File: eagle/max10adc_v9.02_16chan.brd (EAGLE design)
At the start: 170 x 79 mm, 533 parts, among them IC1 MAX11115AUT+T, IC10 MAX11115AUT+T, IC11 MAX11115AUT+T, IC12 MAX11115AUT+T, IC13 MAX11115AUT+T, IC14 MAX11115AUT+T, IC15 MAX11115AUT+T, IC16 MAX11115AUT+T, IC2 MAX11115AUT+T, IC21 MAX11115AUT+T, IC22 MAX11115AUT+T, IC23 MAX11115AUT+T, IC24 MAX11115AUT+T, IC3 MAX11115AUT+T, IC4 MAX11115AUT+T, IC9 MAX11115AUT+T, K1 AQY21SOP, K10 AQY21SOP, K11 AQY21SOP, K12 AQY21SOP, K13 AQY21SOP, K14 AQY21SOP, K15 AQY21SOP, K16 AQY21SOP, K21 AQY21SOP, K22 AQY21SOP, K23 AQY21SOP, K24 AQY21SOP, K3 AQY21SOP, K5 AQY21SOP, K6 AQY21SOP, K9 AQY21SOP, U340G CH340G, X1 LTI-SASF54GT, X10 LTI-SASF54GT, X11 LTI-SASF54GT, X12 LTI-SASF54GT, X13 LTI-SASF54GT, X14 LTI-SASF54GT, X15 LTI-SASF54GT, X16 LTI-SASF54GT, X21 LTI-SASF54GT, X22 LTI-SASF54GT, X23 LTI-SASF54GT, X24 LTI-SASF54GT, X4 LTI-SASF54GT, X5 LTI-SASF54GT, X6 LTI-SASF54GT, X9 LTI-SASF54GT, Y1 ABL-12.000MHZ-B2

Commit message: MAX11105
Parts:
- IC1, IC10, IC11, IC12, IC13, IC14, IC15, IC16, IC2, IC21, IC22, IC23, IC24, IC3, IC4, IC9: value MAX11115AUT+T -> MAX11105AUT+T

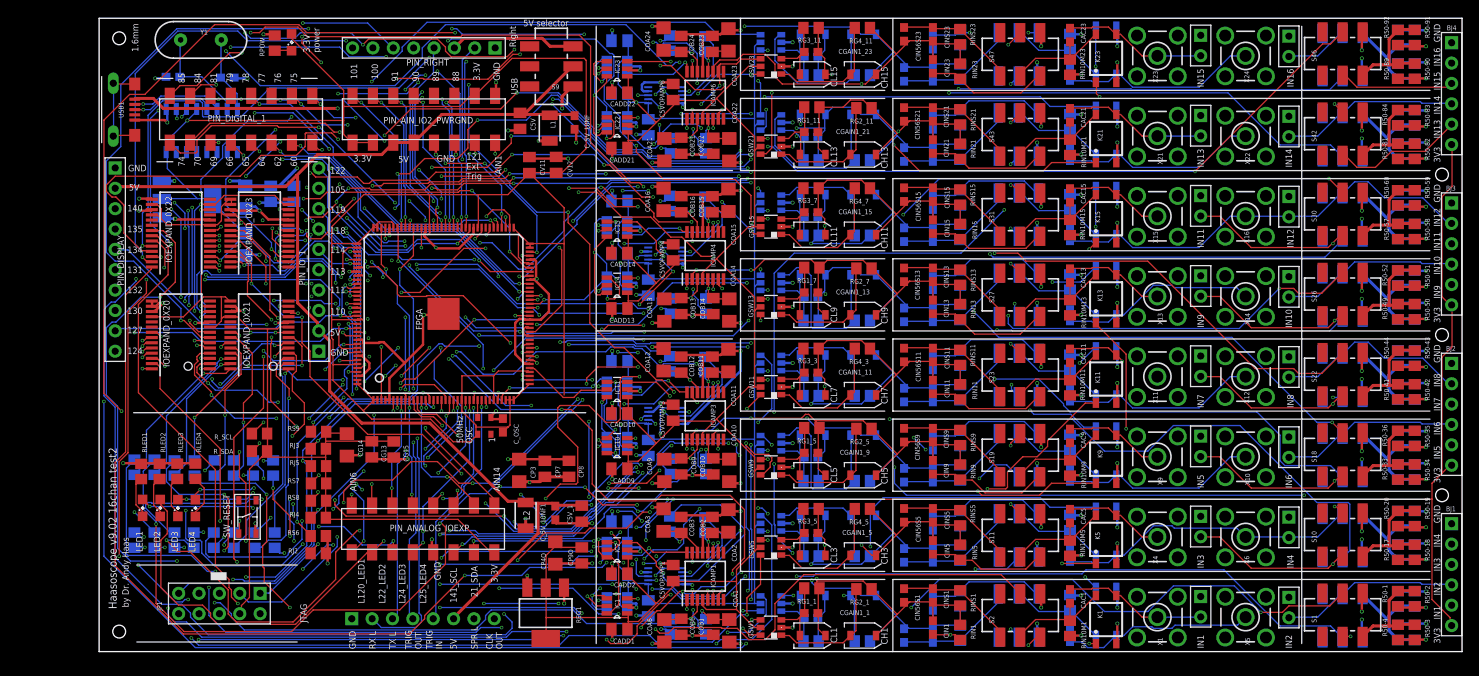
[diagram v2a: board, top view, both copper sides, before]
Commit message: with 24pF fixed caps
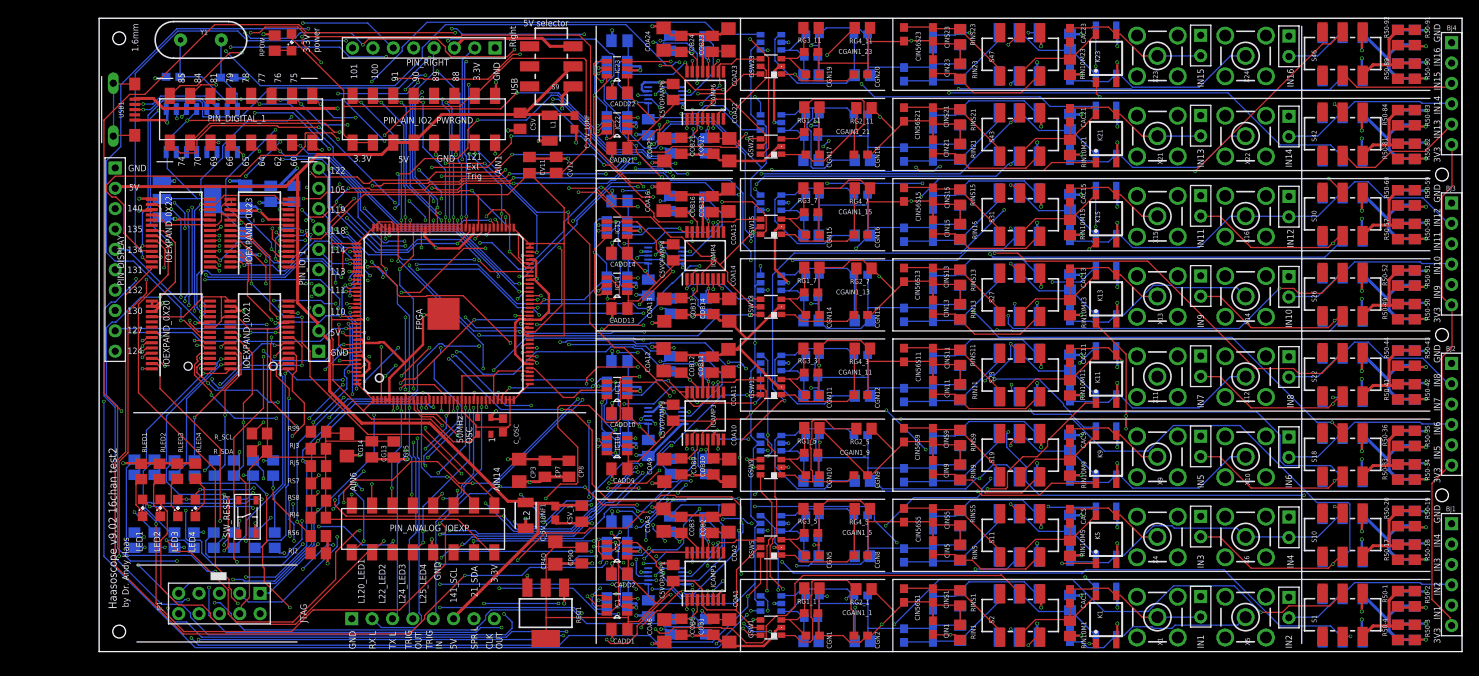
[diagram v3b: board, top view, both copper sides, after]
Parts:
- removed CH1, CH10, CH11, CH12, CH13, CH14, CH15, CH16, CH2, CH3, CH4, CH5, CH6, CH7, CH8, CH9, CL1, CL10, CL11, CL12, CL13, CL14, CL15, CL16, CL2, CL3, CL4, CL5, CL6, CL7, CL8, CL9: 8-45pF, SparkFun-Passives:CTZ3
- added CGN1, CGN10, CGN11, CGN12, CGN13, CGN14, CGN15, CGN16, CGN17, CGN18, CGN19, CGN2, CGN20, CGN21, CGN22, CGN23, CGN24, CGN25, CGN26, CGN27, CGN28, CGN29, CGN3, CGN30, CGN31, CGN32, CGN4, CGN5, CGN6, CGN7, CGN8, CGN9: 24pF, rcl@1:C0603
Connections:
- net CGAIN1: now also CGN1.2; no longer CL1.-
- net CGAIN10: now also CGN8.2; no longer CH3.-
- net CGAIN11: now also CGN6.1; no longer CL4.-
- net CGAIN12: now also CGN7.2; no longer CH4.-
- net CGAIN17: now also CGN10.2; no longer CL5.-
- net CGAIN18: now also CGN9.2; no longer CH5.-
- net CGAIN19: now also CGN22.2; no longer CL6.-
- net CGAIN2: now also CGN2.2; no longer CH1.-
- net CGAIN20: now also CGN21.2; no longer CH6.-
- net CGAIN21: now also CGN11.1; no longer CL7.-
- net CGAIN22: now also CGN12.1; no longer CH7.-
- net CGAIN23: now also CGN23.1; no longer CL8.-
- net CGAIN24: now also CGN24.1; no longer CH8.-
- net CGAIN25: now also CGN14.2; no longer CL9.-
- net CGAIN26: now also CGN13.2; no longer CH9.-
- net CGAIN27: now also CGN26.2; no longer CL10.-
- net CGAIN28: now also CGN25.2; no longer CH10.-
- net CGAIN29: now also CGN15.1; no longer CL11.-
- net CGAIN30: now also CGN16.1; no longer CH11.-
- net CGAIN31: now also CGN27.1; no longer CL12.-
- net CGAIN32: now also CGN28.1; no longer CH12.-
- net CGAIN41: now also CGN18.2; no longer CL13.-
- net CGAIN42: now also CGN17.2; no longer CH13.-
- net CGAIN43: now also CGN30.2; no longer CL14.-
- net CGAIN44: now also CGN29.2; no longer CH14.-
- net CGAIN45: now also CGN19.1; no longer CL15.-
- net CGAIN46: now also CGN20.1; no longer CH15.-
- net CGAIN47: now also CGN31.1; no longer CL16.-
- net CGAIN48: now also CGN32.1; no longer CH16.-
- net CGAIN5: now also CGN4.2; no longer CL2.-
- net CGAIN6: now also CGN3.2; no longer CH2.-
- net CGAIN9: now also CGN5.1; no longer CL3.-
- net INAMINUS1: now also CGN1.1, CGN2.1; no longer CH1.+, CL1.+
- net INAMINUS10: now also CGN25.1, CGN26.1; no longer CH10.+, CL10.+
- net INAMINUS11: now also CGN15.2, CGN16.2; no longer CH11.+, CL11.+
- net INAMINUS12: now also CGN27.2, CGN28.2; no longer CH12.+, CL12.+
- net INAMINUS13: now also CGN17.1, CGN18.1; no longer CH13.+, CL13.+
- net INAMINUS14: now also CGN29.1, CGN30.1; no longer CH14.+, CL14.+
- net INAMINUS15: now also CGN19.2, CGN20.2; no longer CH15.+, CL15.+
- net INAMINUS16: now also CGN31.2, CGN32.2; no longer CH16.+, CL16.+
- net INAMINUS2: now also CGN3.1, CGN4.1; no longer CH2.+, CL2.+
- net INAMINUS3: now also CGN5.2, CGN8.1; no longer CH3.+, CL3.+
- net INAMINUS4: now also CGN6.2, CGN7.1; no longer CH4.+, CL4.+
- net INAMINUS5: now also CGN10.1, CGN9.1; no longer CH5.+, CL5.+
- net INAMINUS6: now also CGN21.1, CGN22.1; no longer CH6.+, CL6.+
- net INAMINUS7: now also CGN11.2, CGN12.2; no longer CH7.+, CL7.+
- net INAMINUS8: now also CGN23.2, CGN24.2; no longer CH8.+, CL8.+
- net INAMINUS9: now also CGN13.1, CGN14.1; no longer CH9.+, CL9.+
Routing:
- net VCCA: track 570.5 -> 518.4 mm, vias 1 -> 8
- net GND: track 607.2 -> 641.1 mm, vias 202 -> 188
- net E_SS10: track 120.3 -> 134.1 mm, vias 7 -> 10
- net CGAIN41: track 9.37 -> 21.5 mm
- net E_GSW5: track 146.6 -> 134.8 mm, vias 5 -> 4
- net INAMINUS11: track 52.2 -> 63.1 mm
- net CGAIN24: track 14.8 -> 25.0 mm
- net CGAIN32: track 14.8 -> 25.0 mm
- net N$8: track 131.7 -> 141.7 mm, vias 4 -> 6
- net E_50SW15: track 198.4 -> 208.4 mm, vias 7 -> 8
- net INAMINUS13: track 65.3 -> 55.8 mm, vias 2 -> 3
- net E_SS12: track 101.9 -> 110.8 mm, vias 5 -> 6
- net CGAIN2: track 15.6 -> 24.4 mm
- net CGAIN18: track 15.6 -> 23.6 mm
- net CGAIN28: track 23.5 -> 15.6 mm
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
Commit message: test3
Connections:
- net N$48 renamed 5VC3
- net N$49 renamed 5VC5
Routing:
- net GND: track 641.1 -> 414.5 mm, vias 188 -> 258
- net +3V3: track 456.1 -> 364.5 mm, vias 2 -> 15
- net E_GSW10: track 86.8 -> 156.9 mm, vias 7 -> 4
- net E_GSW5: track 134.8 -> 87.9 mm, vias 4 -> 6
- net E_GSW11: track 98.4 -> 144.5 mm, vias 8 -> 3
- net E_50SW2: track 204.0 -> 248.9 mm, vias 6 -> 10
- net E_50SW6: track 244.1 -> 203.1 mm, vias 6 -> 7
- net E_50SW7: track 205.3 -> 165.1 mm, vias 6 -> 8
- net E_SS4: track 176.9 -> 137.6 mm, vias 7 -> 8
- net E_GSW7: track 103.9 -> 142.4 mm, vias 3 -> 5
- net E_50SW10: track 152.8 -> 190.8 mm, vias 7 -> 6
- net VCCA: track 518.4 -> 556.3 mm, vias 8 -> 1
- net E_SS10: track 134.1 -> 96.4 mm, vias 10 -> 6
- net N$37: track 134.5 -> 170.7 mm
- net E_GSW13: track 131.4 -> 96.1 mm, vias 6 -> 9
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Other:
- board text added: "Haasoscope v9.02 16chan test3"
- board text removed: "Haasoscope v9.02 16chan test2"

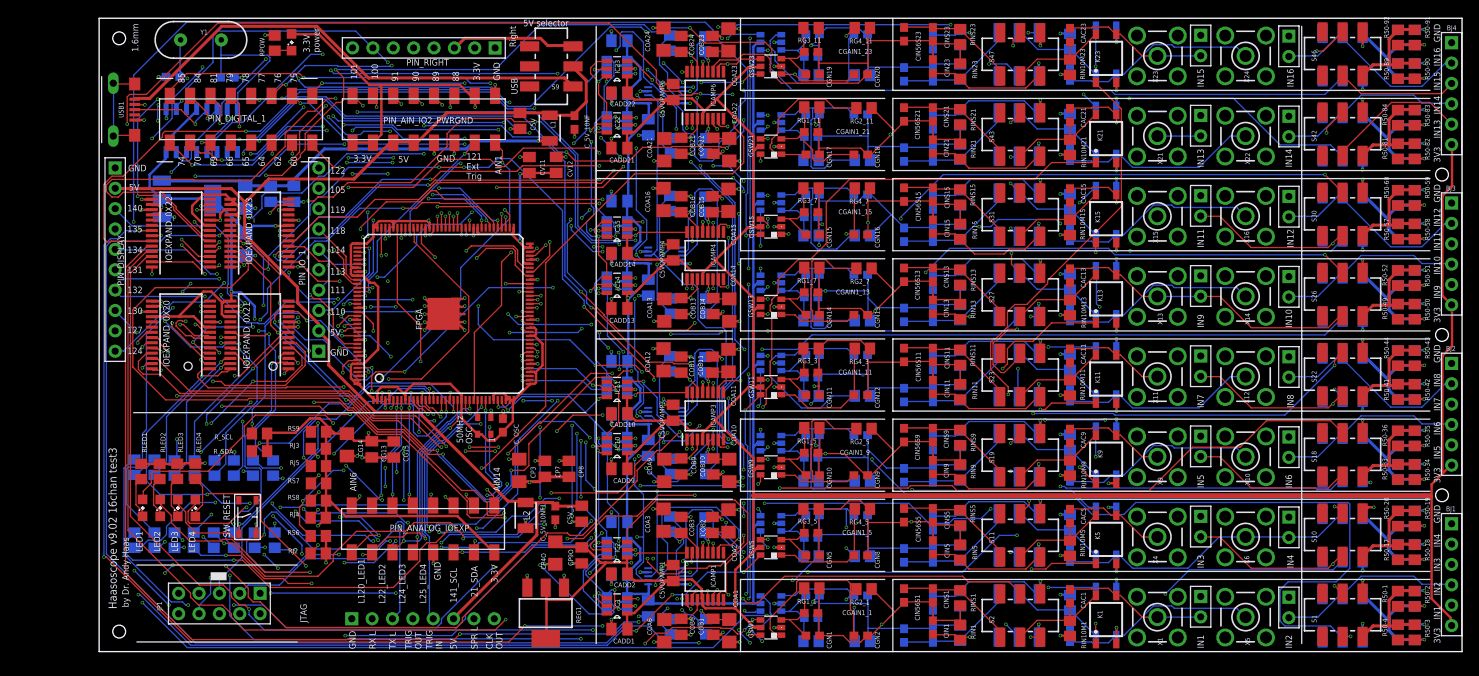
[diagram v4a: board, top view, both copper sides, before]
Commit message: front panel with 50 Ohm termination and SMAs
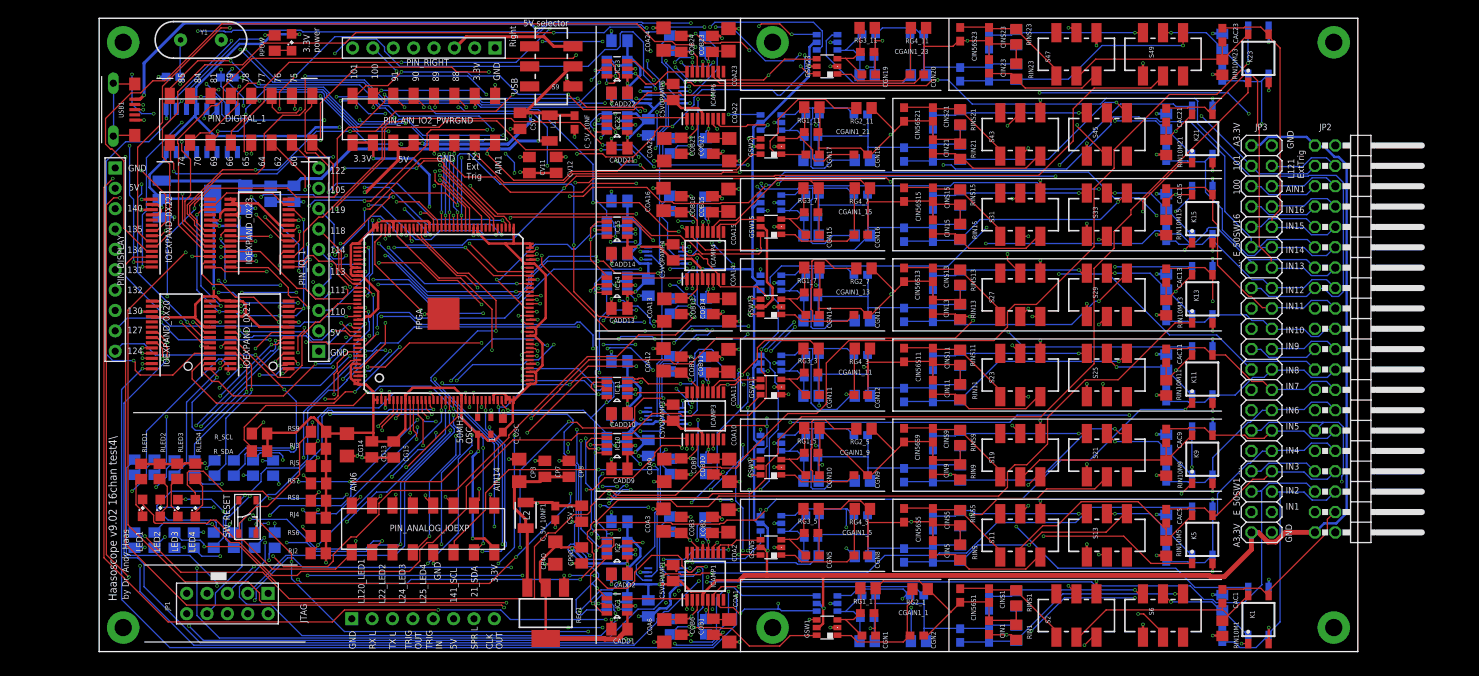
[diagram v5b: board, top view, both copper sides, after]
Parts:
- removed BJ1, BJ2, BJ3, BJ4: 6p-2.54, Seeed-Connector:H6-2.54
- removed IN1, IN10, IN11, IN12, IN13, IN14, IN15, IN16, IN2, IN3, IN4, IN5, IN6, IN7, IN8, IN9: 2p-2.54, Seeed-Connector:H2-2.54
- removed R50-1, R50-10, R50-11, R50-12, R50-17, R50-18, R50-19, R50-2, R50-20, R50-21, R50-22, R50-23, R50-24, R50-3, R50-33, R50-34, R50-35, R50-36, R50-37, R50-38, R50-39, R50-4, R50-40, R50-41, R50-42, R50-43, R50-44, R50-45, R50-46, R50-47, R50-48, R50-49, R50-50, R50-51, R50-52, R50-53, R50-54, R50-55, R50-56, R50-57, R50-58, R50-59, R50-60, R50-61, R50-62, R50-63, R50-64, R50-81, R50-82, R50-83, R50-84, R50-85, R50-86, R50-87, R50-88, R50-89, R50-9, R50-90, R50-91, R50-92, R50-93, R50-94, R50-95, R50-96: 200R, resistor:R0805
- removed S1, S10, S12, S18, S20, S22, S24, S26, S28, S30, S32, S42, S44, S46, S48, S5: JS202011SCQN, switch-ck:JS202011SCQN
- removed X1, X10, X11, X12, X13, X14, X15, X16, X21, X22, X23, X24, X4, X5, X6, X9: LTI-SASF54GT, con-coax:LTI-SASF54GT
- added H1, H2, H3, H4, H5, H6: STANDOFF_ELECTRICAL, SparkFun-Hardware:STANDOFF-ELECTRICAL
- added JP2: (no value), pinhead:2X20/90
- added JP3: (no value), pinhead:2X20
- moved CAC1 19.0 mm to (128.1, -5.10)
- moved CAC23 19.0 mm to (128.1, 64.9)
- moved CAC24 19.0 mm to (128.1, 60.1)
- moved CAC3 19.0 mm to (128.1, -9.90)
- moved K1 19.0 mm to (132.6, -8.00)
- moved K23 19.0 mm to (132.6, 62.0)
- moved K24 19.0 mm to (132.6, 63.0)
- moved K3 19.0 mm to (132.6, -7.00)
- moved RIN10M1 19.0 mm to (128.1, -9.10)
- moved RIN10M23 19.0 mm to (128.1, 60.9)
- moved RIN10M24 19.0 mm to (128.1, 64.1)
- moved RIN10M3 19.0 mm to (128.1, -5.90)
- moved S49 18.0 mm to (120.7, 62.5), flipped to the top
- moved S6 18.0 mm to (120.7, -7.50), flipped to the top
- moved CAC10 12.0 mm to (121.1, 10.1)
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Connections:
- removed net N50_1: R50-1.1, R50-2.1, R50-3.1, R50-4.1, S1.3
- removed net N50_10: R50-53.1, R50-54.1, R50-55.1, R50-56.1, S28.3
- removed net N50_11: R50-57.1, R50-58.1, R50-59.1, R50-60.1, S30.3
- removed net N50_12: R50-61.1, R50-62.1, R50-63.1, R50-64.1, S32.3
- removed net N50_13: R50-81.1, R50-82.1, R50-83.1, R50-84.1, S42.3
- removed net N50_14: R50-85.1, R50-86.1, R50-87.1, R50-88.1, S44.3
- removed net N50_15: R50-89.1, R50-90.1, R50-91.1, R50-92.1, S46.3
- removed net N50_16: R50-93.1, R50-94.1, R50-95.1, R50-96.1, S48.3
- removed net N50_2: R50-10.1, R50-11.1, R50-12.1, R50-9.1, S5.3
- removed net N50_3: R50-17.1, R50-18.1, R50-19.1, R50-20.1, S10.3
- removed net N50_4: R50-21.1, R50-22.1, R50-23.1, R50-24.1, S12.3
- removed net N50_5: R50-33.1, R50-34.1, R50-35.1, R50-36.1, S18.3
- removed net N50_6: R50-37.1, R50-38.1, R50-39.1, R50-40.1, S20.3
- removed net N50_7: R50-41.1, R50-42.1, R50-43.1, R50-44.1, S22.3
- removed net N50_8: R50-45.1, R50-46.1, R50-47.1, R50-48.1, S24.3
- removed net N50_9: R50-49.1, R50-50.1, R50-51.1, R50-52.1, S26.3
- net AIN1: now also JP2.6, JP3.6
- net E_50SW1: now also JP2.37, JP3.37; no longer S1.5
- net E_50SW10: now also JP2.19, JP3.19; no longer S28.5
- net E_50SW11: now also JP2.17, JP3.17; no longer S30.5
- net E_50SW12: now also JP2.15, JP3.15; no longer S32.5
- net E_50SW13: now also JP2.13, JP3.13; no longer S42.5
- net E_50SW14: now also JP2.11, JP3.11; no longer S44.5
- net E_50SW15: now also JP2.9, JP3.9; no longer S46.5
- net E_50SW16: now also JP2.7, JP3.7; no longer S48.5
- net E_50SW2: now also JP2.35, JP3.35; no longer S5.5
- net E_50SW3: now also JP2.33, JP3.33; no longer S10.5
- net E_50SW4: now also JP2.31, JP3.31; no longer S12.5
- net E_50SW5: now also JP2.29, JP3.29; no longer S18.5
- net E_50SW6: now also JP2.27, JP3.27; no longer S20.5
- net E_50SW7: now also JP2.25, JP3.25; no longer S22.5
- net E_50SW8: now also JP2.23, JP3.23; no longer S24.5
- net E_50SW9: now also JP2.21, JP3.21; no longer S26.5
- net GND: now also H1.P1, H2.P1, H3.P1, H4.P1, H5.P1, H6.P1, JP2.2, JP2.40, JP3.2, JP3.40; no longer BJ1.1, BJ2.1, BJ3.1, BJ4.1, IN1.1, IN10.1, IN11.1, IN12.1, IN13.1, IN14.1, IN15.1, IN16.1, IN2.1, IN3.1, IN4.1, IN5.1, IN6.1, IN7.1, IN8.1, IN9.1, R50-1.2, R50-10.2, R50-11.2, R50-12.2, R50-17.2, R50-18.2, R50-19.2, R50-2.2, R50-20.2, R50-21.2, R50-22.2, R50-23.2, R50-24.2, R50-3.2, R50-33.2, R50-34.2, R50-35.2, R50-36.2, R50-37.2, R50-38.2, R50-39.2, R50-4.2, R50-40.2, R50-41.2, R50-42.2, R50-43.2, R50-44.2, R50-45.2, R50-46.2, R50-47.2, R50-48.2, R50-49.2, R50-50.2, R50-51.2, R50-52.2, R50-53.2, R50-54.2, R50-55.2, R50-56.2, R50-57.2, R50-58.2, R50-59.2, R50-60.2, R50-61.2, R50-62.2, R50-63.2, R50-64.2, R50-81.2, R50-82.2, R50-83.2, R50-84.2, R50-85.2, R50-86.2, R50-87.2, R50-88.2, R50-89.2, R50-9.2, R50-90.2, R50-91.2, R50-92.2, R50-93.2, R50-94.2, R50-95.2, R50-96.2, S1.6, S10.6, S12.6, S18.6, S20.6, S22.6, S24.6, S26.6, S28.6, S30.6, S32.6, S42.6, S44.6, S46.6, S48.6, S5.6, X1.2, X1.3, X1.4, X1.5, X10.2, X10.3, X10.4, X10.5, X11.2, X11.3, X11.4, X11.5, X12.2, X12.3, X12.4, X12.5, X13.2, X13.3, X13.4, X13.5, X14.2, X14.3, X14.4, X14.5, X15.2, X15.3, X15.4, X15.5, X16.2, X16.3, X16.4, X16.5, X21.2, X21.3, X21.4, X21.5, X22.2, X22.3, X22.4, X22.5, X23.2, X23.3, X23.4, X23.5, X24.2, X24.3, X24.4, X24.5, X4.2, X4.3, X4.4, X4.5, X5.2, X5.3, X5.4, X5.5, X6.2, X6.3, X6.4, X6.5, X9.2, X9.3, X9.4, X9.5
- net INJ1: now also JP2.38, JP3.38; no longer BJ1.5, IN1.2, S1.2, X1.1
- net INJ10: now also JP2.20, JP3.20; no longer BJ3.4, IN10.2, S28.2, X14.1
- net INJ11: now also JP2.18, JP3.18; no longer BJ3.3, IN11.2, S30.2, X15.1
- net INJ12: now also JP2.16, JP3.16; no longer BJ3.2, IN12.2, S32.2, X16.1
- net INJ13: now also JP2.14, JP3.14; no longer BJ4.5, IN13.2, S42.2, X21.1
- net INJ14: now also JP2.12, JP3.12; no longer BJ4.4, IN14.2, S44.2, X22.1
- net INJ15: now also JP2.10, JP3.10; no longer BJ4.3, IN15.2, S46.2, X23.1
- net INJ16: now also JP2.8, JP3.8; no longer BJ4.2, IN16.2, S48.2, X24.1
- net INJ2: now also JP2.36, JP3.36; no longer BJ1.4, IN2.2, S5.2, X5.1
- net INJ3: now also JP2.34, JP3.34; no longer BJ1.3, IN3.2, S10.2, X4.1
- net INJ4: now also JP2.32, JP3.32; no longer BJ1.2, IN4.2, S12.2, X6.1
- net INJ5: now also JP2.30, JP3.30; no longer BJ2.5, IN5.2, S18.2, X9.1
- net INJ6: now also JP2.28, JP3.28; no longer BJ2.4, IN6.2, S20.2, X10.1
- net INJ7: now also JP2.26, JP3.26; no longer BJ2.3, IN7.2, S22.2, X11.1
- net INJ8: now also JP2.24, JP3.24; no longer BJ2.2, IN8.2, S24.2, X12.1
- net INJ9: now also JP2.22, JP3.22; no longer BJ3.5, IN9.2, S26.2, X13.1
- net IO_100: now also JP2.5, JP3.5
- net IO_101: now also JP2.3, JP3.3
- net L121: now also JP2.4, JP3.4
- net VCCA: now also JP2.1, JP2.39, JP3.1, JP3.39; no longer BJ1.6, BJ2.6, BJ3.6, BJ4.6
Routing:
- net IO_100: track 19.9 -> 164.6 mm, vias 2 -> 5
- net GND: track 414.5 -> 270.9 mm, vias 258 -> 201
- net IO_101: track 21.6 -> 152.9 mm, vias 2 -> 6
- net AIN1: track 39.5 -> 156.2 mm, vias 3 -> 5
- net L121: track 25.6 -> 141.8 mm, vias 2 -> 3
- net VCCA: track 556.3 -> 450.3 mm, vias 1 -> 20
- net E_GSW10: track 156.9 -> 82.0 mm, vias 4 -> 8
- net E_50SW7: track 165.1 -> 225.7 mm
- net E_GSW11: track 144.5 -> 91.6 mm
- net E_GSW12: track 86.5 -> 137.3 mm, vias 6 -> 5
- net E_SS4: track 137.6 -> 188.0 mm, vias 8 -> 6
- net E_GSW6: track 86.9 -> 137.0 mm
- net INJ5: track 70.3 -> 22.9 mm
- net E_GSW5: track 87.9 -> 133.3 mm, vias 6 -> 4
- net E_50SW5: track 207.0 -> 251.9 mm, vias 4 -> 2
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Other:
- board size 170 x 79 mm -> 157 x 79 mm
- board text added: "... E_50SW16"
- board text added: "A3.3V"
- board text added: "E_50SW1 ..."
- board text added: "Haasoscope v9.02 16chan test4\"
- board text added: "L121 ExtTrig"
- board text removed: "1.6mm"
- board text removed: "3V3"
- board text removed: "Haasoscope v9.02 16chan test3"
